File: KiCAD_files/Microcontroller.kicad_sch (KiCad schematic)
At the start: 58 parts, among them J403 RJE721881411, J404 RJE721881411, U401 OwnTech_SPIN, U402 TCAN334GDR, U405 LTC2850xS8, U406 MCP6487T-E/SN

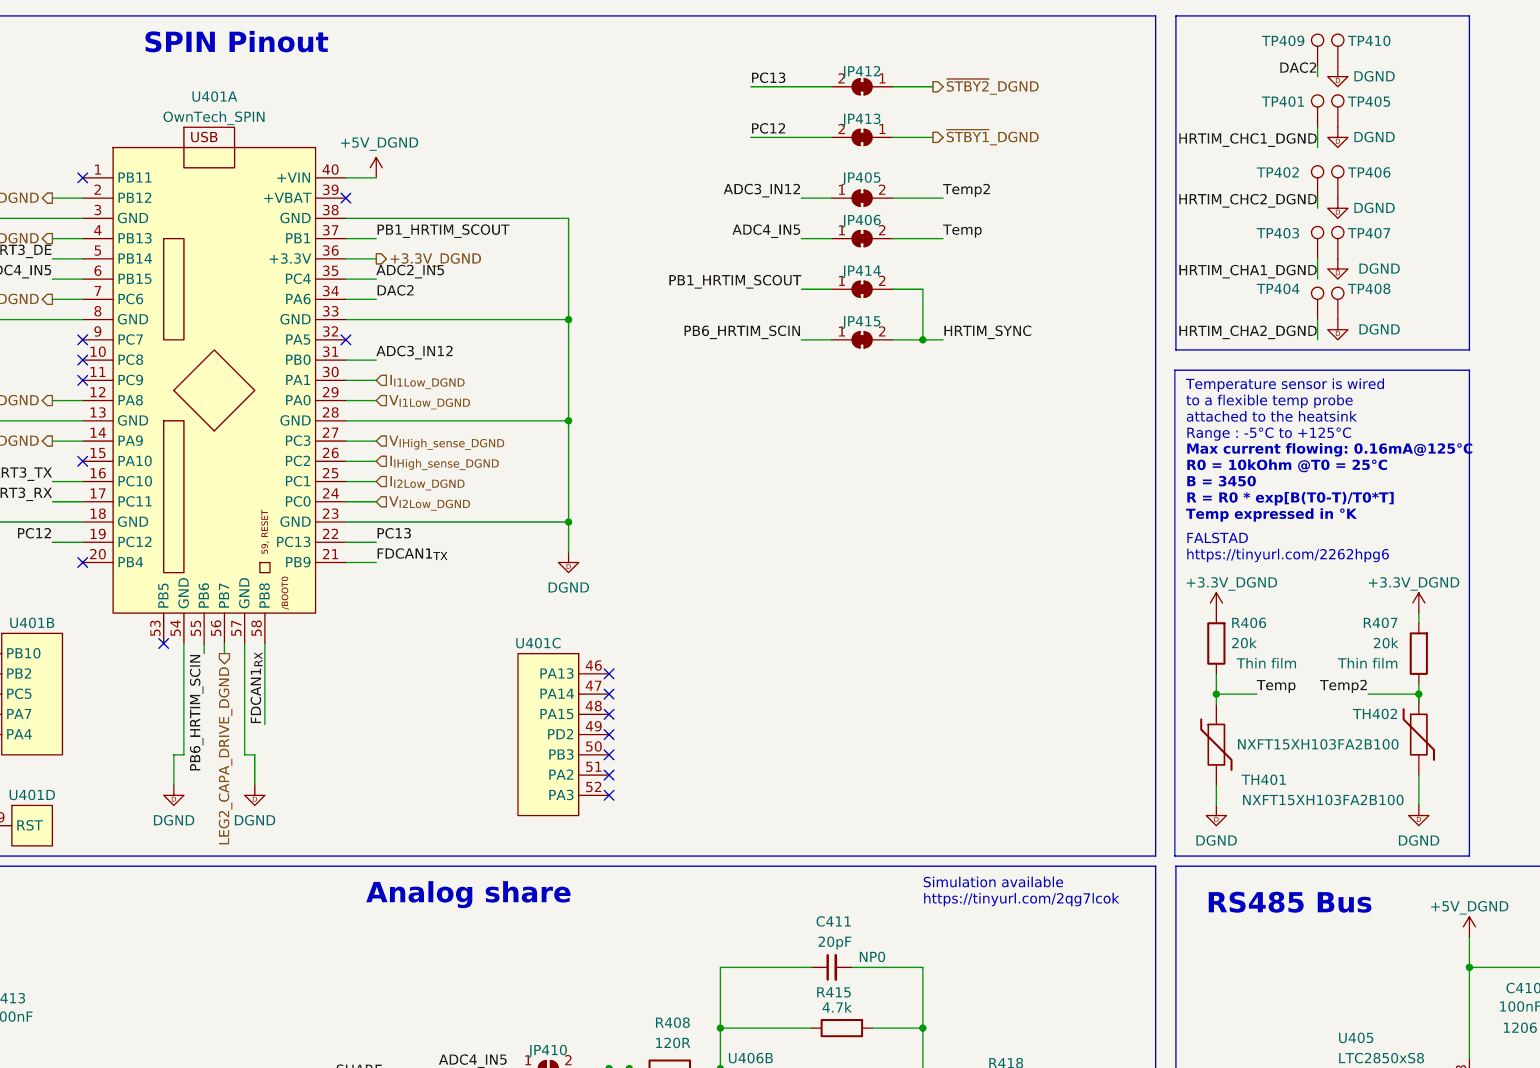
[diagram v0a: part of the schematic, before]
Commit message: better comment on conditionning circuits (VHigh, VLow, Ihigh and ILOW)
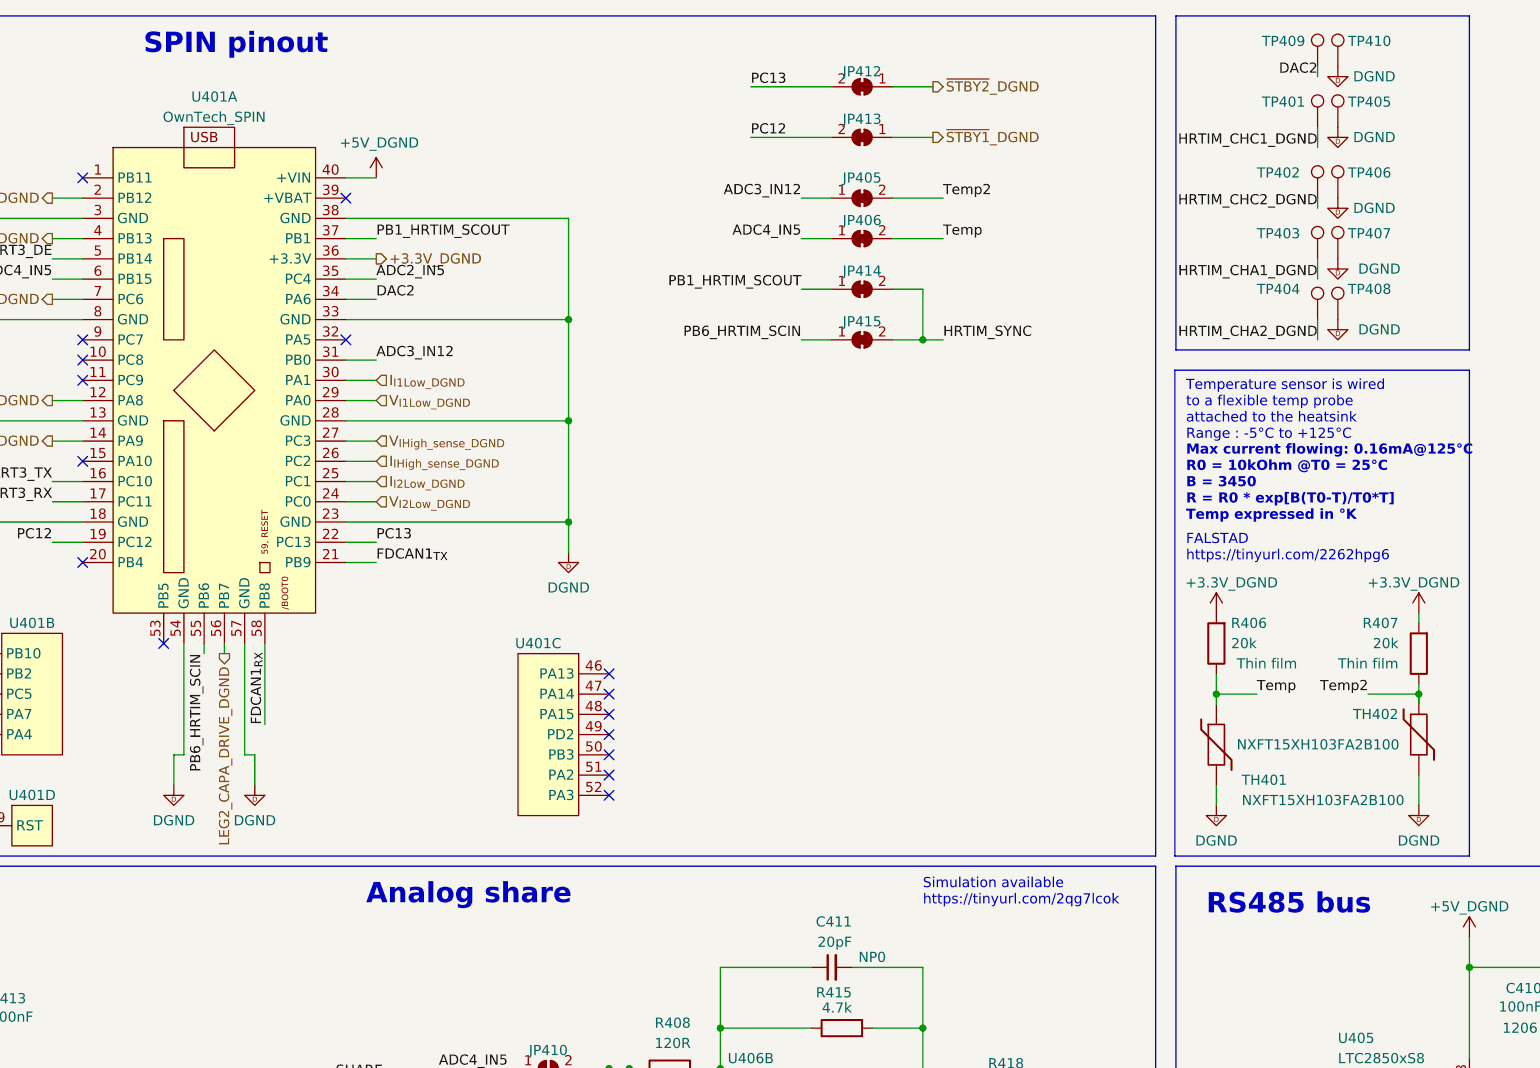
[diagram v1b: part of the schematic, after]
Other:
- note added: "RS485 bus"
- note added: "SPIN pinout"
- note removed: "RS485 Bus"
- note removed: "SPIN Pinout"
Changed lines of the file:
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@@
     (effects (font (face "Arial") (size 1.27 1.27)) (justify left bottom))
   )
-  (text "SPIN Pinout" (at 73.66 19.05 0)
+  (text "SPIN pinout" (at 73.66 19.05 0)
     (effects (font (size 2.54 2.54) (thickness 0.4978) bold) (justify left bottom))
   )
@@
     (effects (font (size 2.4892 2.4892)) (justify left bottom))
   )
-  (text "RS485 Bus" (at 207.01 127 0)
+  (text "RS485 bus" (at 207.01 127 0)
     (effects (font (size 2.54 2.54) (thickness 0.508) bold) (justify left bottom))
   )

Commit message: acquisition chain resistor are now 0.5% tolerance
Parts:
- R406, R407: manf# RT0805FRE1320KL -> RT0805DRD0720KL
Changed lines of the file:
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@@
       (effects (font (size 1.27 1.27)) hide)
     )
-    (property "manf#" "RT0805FRE1320KL" (at 208.28 92.71 0)
+    (property "manf#" "RT0805DRD0720KL" (at 208.28 92.71 0)
       (effects (font (size 1.27 1.27)) hide)
     )
@@
       (effects (font (size 1.27 1.27)) hide)
     )
-    (property "manf#" "RT0805FRE1320KL" (at 233.68 93.98 0)
+    (property "manf#" "RT0805DRD0720KL" (at 233.68 93.98 0)
       (effects (font (size 1.27 1.27)) hide)
     )

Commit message: wip indus
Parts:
- removed C402: 10nF, Footprints:C_0805_2012Metric, symbol Device:C_Small
- removed R402, R404: 330R, Footprints:R_0805_2012Metric, symbol Device:R_Small
- removed R403, R405: 3k, Footprints:R_0805_2012Metric, symbol Device:R_Small
- added C504: 22nF, Footprints:C_0805_2012Metric, symbol Device:C
- added R403, R405: 4.7k, Footprints:R_0805_2012Metric, symbol Device:R
- added R506 (x2): 470R, Footprints:R_0805_2012Metric, symbol Device:R
- C401, C413: footprint Footprints:C_0805_2012Metric -> Capacitor_SMD:C_1206_3216Metric; manf# C0805C104K5RACTU -> C1206C104K5RAC7867
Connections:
- net CAN_L: now also R506.2, R506.2
- net DGND: now also C504.2, R403.2, R405.2
- net at J403.11: now also R506.1
- net at J403.9: now also R403.1
- net at J404.11: now also R506.1
- net at J404.9: now also R405.1
- net at JP410.2 (B), JP411.2 (B), R408.2: now also C504.1
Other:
- note added: "Low pass filter Resistor = 120R Cap = 22nF Cutoff freq = 60 kHz"
- note removed: "Low pass filter Resistor = 120R Cap = 10nF Cutoff freq = 132 kHz"
- moved on the sheet: R408

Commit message: ready for design review
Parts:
- removed R408: 120R, Footprints:R_0805_2012Metric, symbol Device:R
- added R204: 51R, Footprints:R_0805_2012Metric, symbol Device:R
- C401, C413: Package 0805 -> 1206
- D403: value PMEG2010AEJ,115 -> PMEG3010CEJ,115; manf# PMEG2010AEJ,115 -> PMEG3010CEJ,115
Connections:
- net DGND: now also R403.1; no longer R403.2
- net at J403.9: now also R403.2; no longer R403.1
- net at C504.1, JP410.2 (B), JP411.2 (B): now also R204.1
- net at C411.1, R415.1, U406.7: now also R204.2
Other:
- note added: "Low pass filter Resistor = 51R Cap = 22nF Cutoff freq = 142 kHz"
- note removed: "Low pass filter Resistor = 120R Cap = 22nF Cutoff freq = 60 kHz"
- moved on the sheet: C504, R403
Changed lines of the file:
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@@
     (stroke (width 0) (type default))
   )
-  (wire (pts (xy 135.89 146.05) (xy 135.89 154.94))
+  (wire (pts (xy 135.89 146.05) (xy 135.89 156.21))
     (stroke (width 0) (type default))
   )
@@
     (stroke (width 0) (type default))
   )
-  (wire (pts (xy 135.89 162.56) (xy 135.89 165.1))
+  (wire (pts (xy 135.89 163.83) (xy 135.89 170.18))
     (stroke (width 0) (type default))
   )
@@
     (effects (font (size 2.54 2.54) (thickness 0.508) bold) (justify left bottom))
   )
-  (text "Low pass filter\nResistor = 120R\nCap = 22nF\nCutoff freq = 60 kHz"
-    (at 139.7 173.99 0)
+  (text "Low pass filter\nResistor = 51R\nCap = 22nF\nCutoff freq = 142 kHz"
+    (at 140.97 172.72 0)
     (effects (font (face "Arial") (size 1.27 1.27)) (justify left bottom))
   )
@@
       (effects (font (size 1.27 1.27)) hide)
     )
-    (property "Package" "0805" (at 74.93 215.9 0)
+    (property "Package" "1206" (at 74.93 215.9 0)
       (effects (font (size 1.27 1.27)) hide)
     )
@@
     )
   )
-  (symbol (lib_id "Device:C") (at 135.89 158.75 0) (unit 1)
+  (symbol (lib_id "Device:C") (at 135.89 160.02 0) (unit 1)
     (in_bom yes) (on_board yes) (dnp no)
-    (property "Reference" "C504" (at 139.7 157.48 0)
+    (property "Reference" "C504" (at 139.7 158.75 0)
       (effects (font (size 1.27 1.27)) (justify left))
     )
-    (property "Value" "22nF" (at 139.7 160.02 0)
+    (property "Value" "22nF" (at 139.7 161.29 0)
       (effects (font (size 1.27 1.27)) (justify left))
     )
-    (property "Footprint" "Footprints:C_0805_2012Metric" (at 136.8552 162.56 0)
+    (property "Footprint" "Footprints:C_0805_2012Metric" (at 136.8552 163.83 0)
       (effects (font (size 1.27 1.27)) hide)
     )
-    (property "Datasheet" "${KIPRJMOD}\\datasheet\\Samsung_MLCC_1837944-1929650.pdf" (at 135.89 158.75 0)
+    (property "Datasheet" "${KIPRJMOD}\\datasheet\\Samsung_MLCC_1837944-1929650.pdf" (at 135.89 160.02 0)
       (effects (font (size 1.27 1.27)) hide)
     )
-    (property "manf#" "CL21B223KBANNWC" (at 135.89 158.75 0)
+    (property "manf#" "CL21B223KBANNWC" (at 135.89 160.02 0)
       (effects (font (size 1.27 1.27)) hide)
     )
-    (property "Functional Block" "Feeder" (at 135.89 158.75 0)
+    (property "Functional Block" "Feeder" (at 135.89 160.02 0)
       (effects (font (size 1.27 1.27)) hide)
     )
-    (property "Metal content" "BaTiO3" (at 135.89 158.75 0)
+    (property "Metal content" "BaTiO3" (at 135.89 160.02 0)
       (effects (font (size 1.27 1.27)) hide)
     )
-    (property "Subfunction" "+6V / DGND supply" (at 135.89 158.75 0)
+    (property "Subfunction" "+6V / DGND supply" (at 135.89 160.02 0)
       (effects (font (size 1.27 1.27)) hide)
     )
-    (property "Package" "0805" (at 135.89 158.75 0)
+    (property "Package" "0805" (at 135.89 160.02 0)
       (effects (font (size 1.27 1.27)) hide)
     )
-    (property "Dielectric" "X7R" (at 135.89 158.75 0)
+    (property "Dielectric" "X7R" (at 135.89 160.02 0)
       (effects (font (size 1.27 1.27)) hide)
     )
-    (property "Voltage" "50V" (at 135.89 158.75 0)
+    (property "Voltage" "50V" (at 135.89 160.02 0)
       (effects (font (size 1.27 1.27)) hide)
     )
-    (property "Technology" "" (at 135.89 158.75 0)
+    (property "Technology" "" (at 135.89 160.02 0)
       (effects (font (size 1.27 1.27)) hide)
     )
@@
       (effects (font (size 1.27 1.27)) hide)
     )
-    (property "Package" "0805" (at 52.07 138.43 0)
+    (property "Package" "1206" (at 52.07 138.43 0)
       (effects (font (size 1.27 1.27)) hide)
     )
@@
     )
   )
+  (symbol (lib_id "Device:R") (at 140.97 146.05 90) (unit 1)
+    (in_bom yes) (on_board yes) (dnp no)
+    (property "Reference" "R204" (at 142.24 143.51 90)
+      (effects (font (size 1.27 1.27)) (justify left))
+    )
+    (property "Value" "51R" (at 142.24 148.59 90)
+      (effects (font (size 1.27 1.27)) (justify left))
+    )
+    (property "Footprint" "Footprints:R_0805_2012Metric" (at 140.97 147.828 90)
+      (effects (font (size 1.27 1.27)) hide)
+    )
+    (property "Datasheet" "${KIPRJMOD}\\datasheet\\cr-1858361.pdf" (at 140.97 146.05 0)
+      (effects (font (size 1.27 1.27)) hide)
+    )
+    (property "DNP" "" (at 140.97 146.05 0)
+      (effects (font (size 1.27 1.27)) hide)
+    )
+    (property "manf#" "CR0805-FX-51R0ELF" (at 140.97 146.05 0)
+      (effects (font (size 1.27 1.27)) hide)
+    )
+    (property "Functional Block" "Driver" (at 140.97 146.05 0)
+      (effects (font (size 1.27 1.27)) hide)
+    )
+    (property "Metal content" "NiCr" (at 140.97 146.05 0)
+      (effects (font (size 1.27 1.27)) hide)
+    )
+    (property "Subfunction" "Driver input" (at 140.97 146.05 0)
+      (effects (font (size 1.27 1.27)) hide)
+    )
+    (property "Package" "0805" (at 140.97 146.05 0)
+      (effects (font (size 1.27 1.27)) hide)
+    )
+    (property "Technology" "Thick film" (at 140.97 146.05 0)
+      (effects (font (size 1.27 1.27)) hide)
+    )
+    (pin "1")
+    (pin "2")
+    (instances
+      (project "Power"
+        (path "/8d0c1d66-35ef-4a53-a28f-436a11b54f42/b9592210-62fd-48e0-8447-67f645d7d247"
+          (reference "R204") (unit 1)
+        )
+        (path "/8d0c1d66-35ef-4a53-a28f-436a11b54f42/4a11142e-1c8b-45f6-8828-f013379f9fc1"
+          (reference "R304") (unit 1)
+        )
+        (path "/8d0c1d66-35ef-4a53-a28f-436a11b54f42/122c01f4-f23e-4db0-9503-7261d96dc78b"
+          (reference "R408") (unit 1)
+        )
+      )
+    )
+  )
   (symbol (lib_id "Symbols:+3.3V_DGND") (at 271.78 241.3 0) (unit 1)
     (in_bom no) (on_board no) (dnp no)
@@
       (effects (font (size 1.27 1.27)))
     )
-    (property "Value" "PMEG2010AEJ,115" (at 87.63 166.37 0)
+    (property "Value" "PMEG3010CEJ,115" (at 87.63 166.37 0)
       (effects (font (size 1.27 1.27)))
     )
@@
       (effects (font (size 1.27 1.27)) hide)
     )
-    (property "Datasheet" "${KIPRJMOD}\\datasheet\\PMEG2010AEJ-2938779.pdf" (at 90.17 161.29 0)
+    (property "Datasheet" "${KIPRJMOD}\\datasheet\\PMEG3010CEH_PMEG3010CEJ-2891636.pdf" (at 90.17 161.29 0)
       (effects (font (size 1.27 1.27)) hide)
     )
@@
       (effects (font (size 1.27 1.27)) hide)
     )
-    (property "manf#" "PMEG2010AEJ,115" (at 90.17 161.29 0)
+    (property "manf#" "PMEG3010CEJ,115" (at 90.17 161.29 0)
       (effects (font (size 1.27 1.27)) hide)
     )
@@
     )
   )
-  (symbol (lib_id "Device:R") (at 140.97 146.05 270) (mirror x) (unit 1)
-    (in_bom yes) (on_board yes) (dnp no)
-    (property "Reference" "R408" (at 139.065 140.335 90)
-      (effects (font (size 1.27 1.27)) (justify left))
-    )
-    (property "Value" "120R" (at 139.065 142.875 90)
-      (effects (font (size 1.27 1.27)) (justify left))
-    )
-    (property "Footprint" "Footprints:R_0805_2012Metric" (at 140.97 147.828 90)
-      (effects (font (size 1.27 1.27)) hide)
-    )
-    (property "Datasheet" "${KIPRJMOD}\\datasheet\\cr-1858361.pdf" (at 140.97 146.05 0)
-      (effects (font (size 1.27 1.27)) hide)
-    )
-    (property "DNP" "" (at 140.97 146.05 0)
-      (effects (font (size 1.27 1.27)) hide)
-    )
-    (property "manf#" "CR0805-FX-1200ELF" (at 140.97 146.05 0)
-      (effects (font (size 1.27 1.27)) hide)
-    )
-    (property "Functional Block" "Communication" (at 140.97 146.05 0)
-      (effects (font (size 1.27 1.27)) hide)
-    )
-    (property "Metal content" "NiCr" (at 140.97 146.05 0)
-      (effects (font (size 1.27 1.27)) hide)
-    )
-    (property "Subfunction" "Analog bus" (at 140.97 146.05 0)
-      (effects (font (size 1.27 1.27)) hide)
-    )
-    (property "Package" "0805" (at 140.97 146.05 0)
-      (effects (font (size 1.27 1.27)) hide)
-    )
-    (property "Technology" "Thick film" (at 140.97 146.05 0)
-      (effects (font (size 1.27 1.27)) hide)
-    )
-    (pin "1")
-    (pin "2")
-    (instances
-      (project "Power"
-        (path "/8d0c1d66-35ef-4a53-a28f-436a11b54f42/122c01f4-f23e-4db0-9503-7261d96dc78b"
-          (reference "R408") (unit 1)
-        )
-      )
-    )
-  )
   (symbol (lib_id "Symbols:+6V_DGND") (at 271.78 228.6 0) (unit 1)
     (in_bom no) (on_board no) (dnp no) (fields_autoplaced)
@@
     )
   )
-  (symbol (lib_id "Device:R") (at 175.26 223.52 90) (mirror x) (unit 1)
+  (symbol (lib_id "Device:R") (at 175.26 223.52 270) (mirror x) (unit 1)
     (in_bom yes) (on_board yes) (dnp no)
-    (property "Reference" "R403" (at 177.8 220.98 90)
+    (property "Reference" "R403" (at 172.72 220.98 90)
       (effects (font (size 1.27 1.27)) (justify left))
     )
-    (property "Value" "4.7k" (at 176.53 226.06 90)
+    (property "Value" "4.7k" (at 173.99 226.06 90)
       (effects (font (size 1.27 1.27)) (justify left))
     )
-    (property "Footprint" "Footprints:R_0805_2012Metric" (at 175.26 221.742 90)
+    (property "Footprint" "Footprints:R_0805_2012Metric" (at 175.26 225.298 90)
       (effects (font (size 1.27 1.27)) hide)
     )
@@
     )
   )
-  (symbol (lib_id "Symbols:DGND") (at 135.89 165.1 0) (unit 1)
+  (symbol (lib_id "Symbols:DGND") (at 135.89 170.18 0) (unit 1)
     (in_bom yes) (on_board yes) (dnp no)
-    (property "Reference" "#PWR0418" (at 135.89 171.45 0)
+    (property "Reference" "#PWR0418" (at 135.89 176.53 0)
       (effects (font (size 1.27 1.27)) hide)
     )
-    (property "Value" "DGND" (at 133.35 168.91 0)
+    (property "Value" "DGND" (at 133.35 173.99 0)
       (effects (font (size 1.27 1.27)) (justify left))
     )
-    (property "Footprint" "" (at 135.89 165.1 0)
+    (property "Footprint" "" (at 135.89 170.18 0)
       (effects (font (size 1.27 1.27)) hide)
     )
-    (property "Datasheet" "" (at 135.89 165.1 0)
+    (property "Datasheet" "" (at 135.89 170.18 0)
       (effects (font (size 1.27 1.27)) hide)
     )
